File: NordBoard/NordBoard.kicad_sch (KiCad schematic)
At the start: 3 parts

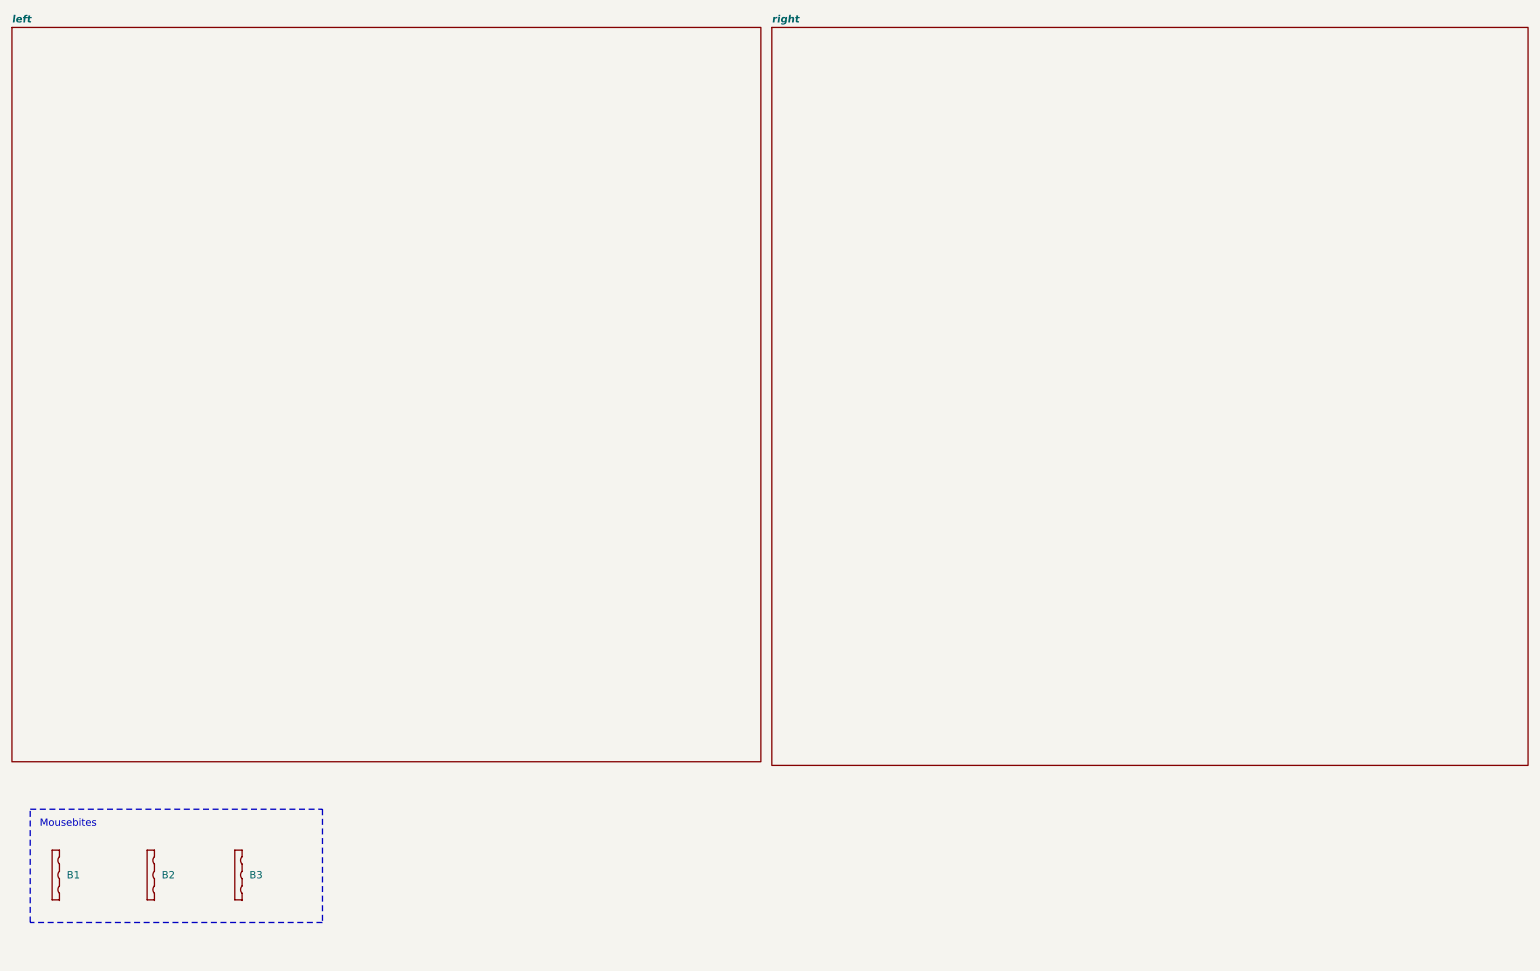
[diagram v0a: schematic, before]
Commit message: feat: implement mousebites
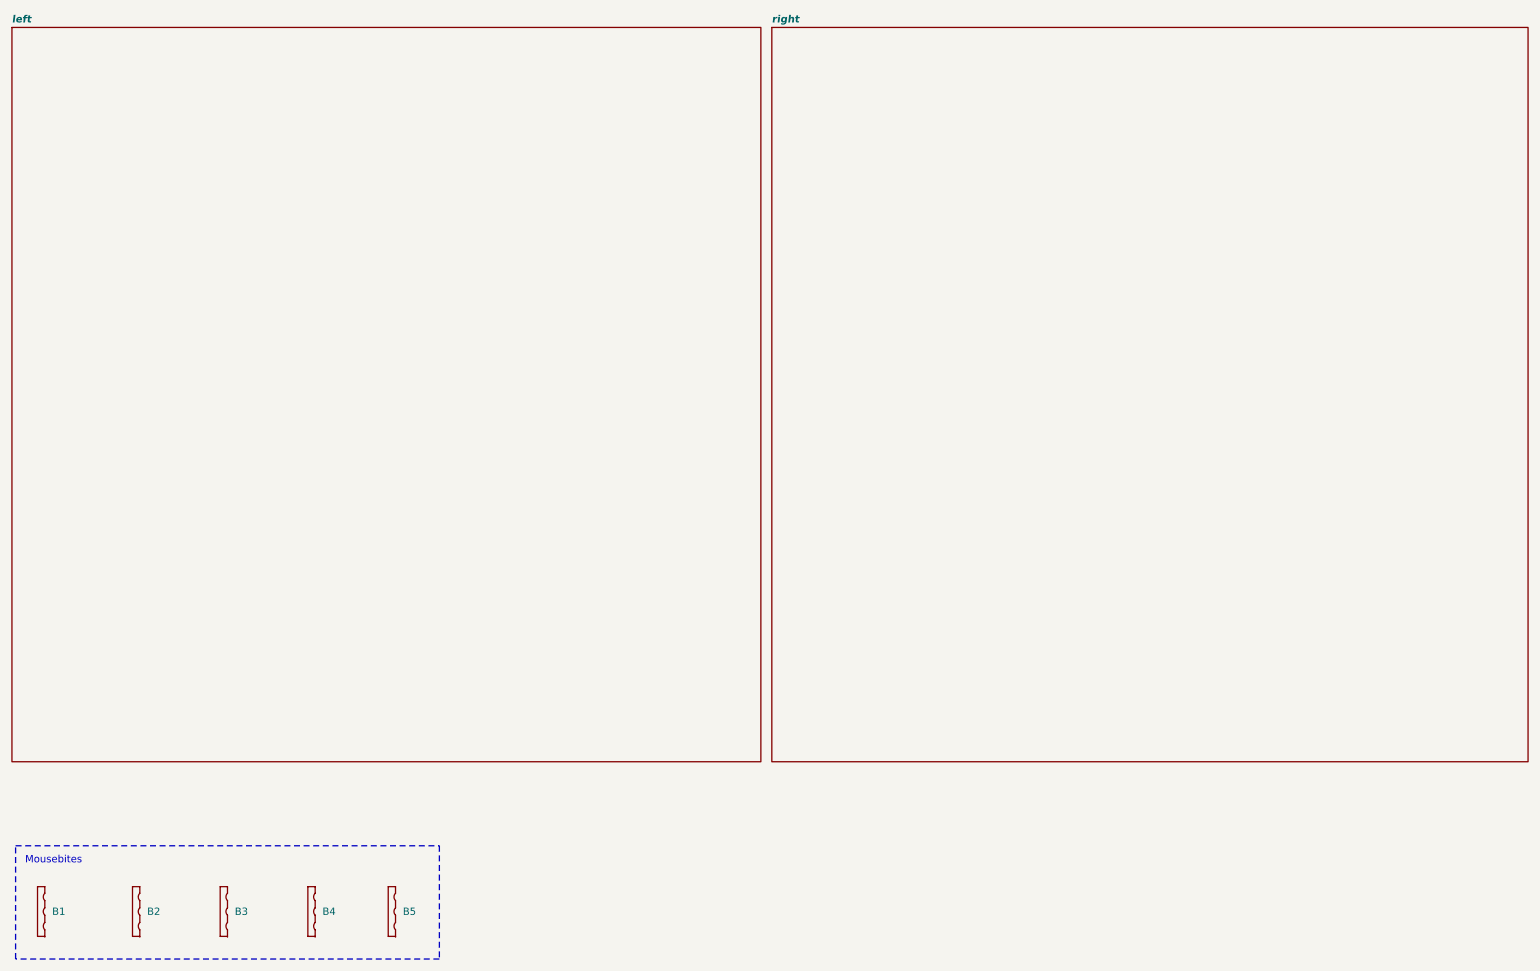
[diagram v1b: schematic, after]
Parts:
- added B4, B5: MouseBite, PCM_marbastlib-various:mousebites_2mm, symbol Mechanical:MouseBite
- B1, B2, B3: footprint Panelization:mouse-bite-5mm-slot -> PCM_marbastlib-various:mousebites_2mm
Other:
- moved on the sheet: B1, B2, B3
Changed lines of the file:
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@@
 	(paper "A4")
 	(rectangle
-		(start 19.05 165.1)
-		(end 69.85 184.785)
+		(start 16.51 171.45)
+		(end 90.17 191.135)
 		(stroke
 			(width 0)
@@
 	(text "Mousebites"
 		(exclude_from_sim no)
-		(at 25.654 167.64 0)
+		(at 23.114 173.99 0)
 		(effects
 			(font
@@
 	(symbol
 		(lib_id "Mechanical:MouseBite")
-		(at 54.61 176.53 0)
+		(at 52.07 182.88 0)
 		(unit 1)
 		(exclude_from_sim yes)
@@
 		(dnp no)
 		(property "Reference" "B3"
-			(at 57.15 176.53 0)
+			(at 54.61 182.88 0)
 			(effects
 				(font
@@
 		)
 		(property "Value" "MouseBite"
-			(at 57.15 177.8624 0)
-			(effects
-				(font
-					(size 1.27 1.27)
-				)
-				(justify left)
-				(hide yes)
-			)
-		)
-		(property "Footprint" "Panelization:mouse-bite-5mm-slot"
-			(at 54.61 176.53 0)
+			(at 54.61 184.2124 0)
+			(effects
+				(font
+					(size 1.27 1.27)
+				)
+				(justify left)
+				(hide yes)
+			)
+		)
+		(property "Footprint" "PCM_marbastlib-various:mousebites_2mm"
+			(at 52.07 182.88 0)
 			(effects
 				(font
@@
 		)
 		(property "Datasheet" "~"
-			(at 54.61 176.53 0)
+			(at 52.07 182.88 0)
 			(effects
 				(font
@@
 		)
 		(property "Description" "Mouse bites, break lines"
-			(at 54.61 176.53 0)
+			(at 52.07 182.88 0)
 			(effects
 				(font
@@
 	(symbol
 		(lib_id "Mechanical:MouseBite")
-		(at 39.37 176.53 0)
+		(at 36.83 182.88 0)
 		(unit 1)
 		(exclude_from_sim yes)
@@
 		(dnp no)
 		(property "Reference" "B2"
-			(at 41.91 176.53 0)
+			(at 39.37 182.88 0)
 			(effects
 				(font
@@
 		)
 		(property "Value" "MouseBite"
-			(at 41.91 177.8624 0)
-			(effects
-				(font
-					(size 1.27 1.27)
-				)
-				(justify left)
-				(hide yes)
-			)
-		)
-		(property "Footprint" "Panelization:mouse-bite-5mm-slot"
-			(at 39.37 176.53 0)
+			(at 39.37 184.2124 0)
+			(effects
+				(font
+					(size 1.27 1.27)
+				)
+				(justify left)
+				(hide yes)
+			)
+		)
+		(property "Footprint" "PCM_marbastlib-various:mousebites_2mm"
+			(at 36.83 182.88 0)
 			(effects
 				(font
@@
 		)
 		(property "Datasheet" "~"
-			(at 39.37 176.53 0)
+			(at 36.83 182.88 0)
 			(effects
 				(font
@@
 		)
 		(property "Description" "Mouse bites, break lines"
-			(at 39.37 176.53 0)
+			(at 36.83 182.88 0)
 			(effects
 				(font
@@
 	(symbol
 		(lib_id "Mechanical:MouseBite")
-		(at 22.86 176.53 0)
+		(at 20.32 182.88 0)
 		(unit 1)
 		(exclude_from_sim yes)
@@
 		(dnp no)
 		(property "Reference" "B1"
-			(at 25.4 176.53 0)
+			(at 22.86 182.88 0)
 			(effects
 				(font
@@
 		)
 		(property "Value" "MouseBite"
-			(at 25.4 177.8624 0)
-			(effects
-				(font
-					(size 1.27 1.27)
-				)
-				(justify left)
-				(hide yes)
-			)
-		)
-		(property "Footprint" "Panelization:mouse-bite-5mm-slot"
-			(at 22.86 176.53 0)
+			(at 22.86 184.2124 0)
+			(effects
+				(font
+					(size 1.27 1.27)
+				)
+				(justify left)
+				(hide yes)
+			)
+		)
+		(property "Footprint" "PCM_marbastlib-various:mousebites_2mm"
+			(at 20.32 182.88 0)
 			(effects
 				(font
@@
 		)
 		(property "Datasheet" "~"
-			(at 22.86 176.53 0)
+			(at 20.32 182.88 0)
 			(effects
 				(font
@@
 		)
 		(property "Description" "Mouse bites, break lines"
-			(at 22.86 176.53 0)
+			(at 20.32 182.88 0)
 			(effects
 				(font
@@
 				(path "/7cf7f72d-7ab1-4807-b592-339093d5ca44"
 					(reference "B1")
+					(unit 1)
+				)
+			)
+		)
+	)
+	(symbol
+		(lib_id "Mechanical:MouseBite")
+		(at 81.28 182.88 0)
+		(unit 1)
+		(exclude_from_sim yes)
+		(in_bom no)
+		(on_board yes)
+		(dnp no)
+		(property "Reference" "B5"
+			(at 83.82 182.88 0)
+			(effects
+				(font
+					(size 1.27 1.27)
+				)
+				(justify left)
+			)
+		)
+		(property "Value" "MouseBite"
+			(at 83.82 184.2124 0)
+			(effects
+				(font
+					(size 1.27 1.27)
+				)
+				(justify left)
+				(hide yes)
+			)
+		)
+		(property "Footprint" "PCM_marbastlib-various:mousebites_2mm"
+			(at 81.28 182.88 0)
+			(effects
+				(font
+					(size 1.27 1.27)
+				)
+				(hide yes)
+			)
+		)
+		(property "Datasheet" "~"
+			(at 81.28 182.88 0)
+			(effects
+				(font
+					(size 1.27 1.27)
+				)
+				(hide yes)
+			)
+		)
+		(property "Description" "Mouse bites, break lines"
+			(at 81.28 182.88 0)
+			(effects
+				(font
+					(size 1.27 1.27)
+				)
+				(hide yes)
+			)
+		)
+		(instances
+			(project "NordBoard"
+				(path "/7cf7f72d-7ab1-4807-b592-339093d5ca44"
+					(reference "B5")
+					(unit 1)
+				)
+			)
+		)
+	)
+	(symbol
+		(lib_id "Mechanical:MouseBite")
+		(at 67.31 182.88 0)
+		(unit 1)
+		(exclude_from_sim yes)
+		(in_bom no)
+		(on_board yes)
+		(dnp no)
+		(property "Reference" "B4"
+			(at 69.85 182.88 0)
+			(effects
+				(font
+					(size 1.27 1.27)
+				)
+				(justify left)
+			)
+		)
+		(property "Value" "MouseBite"
+			(at 69.85 184.2124 0)
+			(effects
+				(font
+					(size 1.27 1.27)
+				)
+				(justify left)
+				(hide yes)
+			)
+		)
+		(property "Footprint" "PCM_marbastlib-various:mousebites_2mm"
+			(at 67.31 182.88 0)
+			(effects
+				(font
+					(size 1.27 1.27)
+				)
+				(hide yes)
+			)
+		)
+		(property "Datasheet" "~"
+			(at 67.31 182.88 0)
+			(effects
+				(font
+					(size 1.27 1.27)
+				)
+				(hide yes)
+			)
+		)
+		(property "Description" "Mouse bites, break lines"
+			(at 67.31 182.88 0)
+			(effects
+				(font
+					(size 1.27 1.27)
+				)
+				(hide yes)
+			)
+		)
+		(instances
+			(project "NordBoard"
+				(path "/7cf7f72d-7ab1-4807-b592-339093d5ca44"
+					(reference "B4")
 					(unit 1)
 				)
@@
 	(sheet
 		(at 147.955 29.21)
-		(size 131.445 128.27)
+		(size 131.445 127.635)
 		(exclude_from_sim no)
 		(in_bom yes)
@@
 		)
 		(property "Sheetfile" "side.kicad_sch"
-			(at 147.955 158.0646 0)
-			(effects
-				(font
+			(at 147.955 157.4296 0)
+			(effects
+				(font

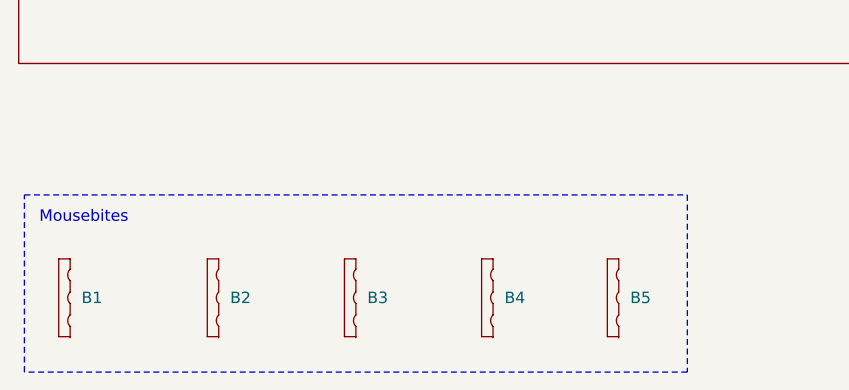
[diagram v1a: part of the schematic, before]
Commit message: feat: finish PCB awaiting peer review + silkscreen
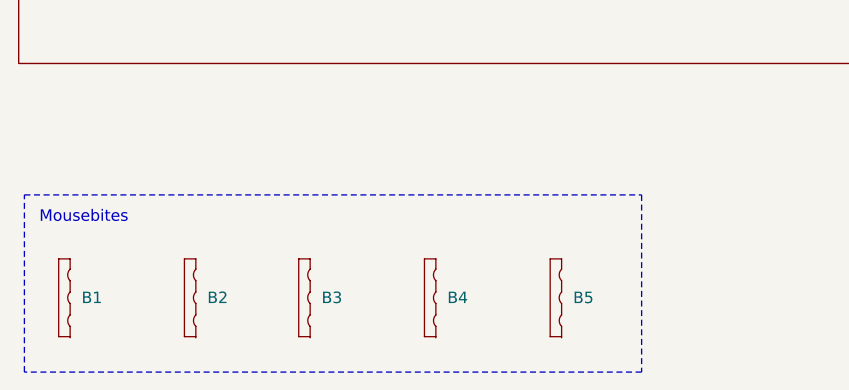
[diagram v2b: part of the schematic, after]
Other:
- moved on the sheet: B2, B3, B4, B5
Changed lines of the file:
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@@
 	(rectangle
 		(start 16.51 171.45)
-		(end 90.17 191.135)
+		(end 85.09 191.135)
 		(stroke
 			(width 0)
@@
 	(symbol
 		(lib_id "Mechanical:MouseBite")
-		(at 52.07 182.88 0)
+		(at 46.99 182.88 0)
 		(unit 1)
 		(exclude_from_sim yes)
@@
 		(dnp no)
 		(property "Reference" "B3"
-			(at 54.61 182.88 0)
-			(effects
-				(font
-					(size 1.27 1.27)
-				)
-				(justify left)
-			)
-		)
-		(property "Value" "MouseBite"
-			(at 54.61 184.2124 0)
-			(effects
-				(font
-					(size 1.27 1.27)
-				)
-				(justify left)
-				(hide yes)
-			)
-		)
-		(property "Footprint" "PCM_marbastlib-various:mousebites_2mm"
-			(at 52.07 182.88 0)
-			(effects
-				(font
-					(size 1.27 1.27)
-				)
-				(hide yes)
-			)
-		)
-		(property "Datasheet" "~"
-			(at 52.07 182.88 0)
-			(effects
-				(font
-					(size 1.27 1.27)
-				)
-				(hide yes)
-			)
-		)
-		(property "Description" "Mouse bites, break lines"
-			(at 52.07 182.88 0)
+			(at 49.53 182.88 0)
+			(effects
+				(font
+					(size 1.27 1.27)
+				)
+				(justify left)
+			)
+		)
+		(property "Value" "MouseBite"
+			(at 49.53 184.2124 0)
+			(effects
+				(font
+					(size 1.27 1.27)
+				)
+				(justify left)
+				(hide yes)
+			)
+		)
+		(property "Footprint" "PCM_marbastlib-various:mousebites_2mm"
+			(at 46.99 182.88 0)
+			(effects
+				(font
+					(size 1.27 1.27)
+				)
+				(hide yes)
+			)
+		)
+		(property "Datasheet" "~"
+			(at 46.99 182.88 0)
+			(effects
+				(font
+					(size 1.27 1.27)
+				)
+				(hide yes)
+			)
+		)
+		(property "Description" "Mouse bites, break lines"
+			(at 46.99 182.88 0)
 			(effects
 				(font
@@
 	(symbol
 		(lib_id "Mechanical:MouseBite")
-		(at 36.83 182.88 0)
+		(at 34.29 182.88 0)
 		(unit 1)
 		(exclude_from_sim yes)
@@
 		(dnp no)
 		(property "Reference" "B2"
-			(at 39.37 182.88 0)
-			(effects
-				(font
-					(size 1.27 1.27)
-				)
-				(justify left)
-			)
-		)
-		(property "Value" "MouseBite"
-			(at 39.37 184.2124 0)
-			(effects
-				(font
-					(size 1.27 1.27)
-				)
-				(justify left)
-				(hide yes)
-			)
-		)
-		(property "Footprint" "PCM_marbastlib-various:mousebites_2mm"
 			(at 36.83 182.88 0)
 			(effects
@@
 					(size 1.27 1.27)
 				)
-				(hide yes)
-			)
-		)
-		(property "Datasheet" "~"
-			(at 36.83 182.88 0)
-			(effects
-				(font
-					(size 1.27 1.27)
-				)
-				(hide yes)
-			)
-		)
-		(property "Description" "Mouse bites, break lines"
-			(at 36.83 182.88 0)
+				(justify left)
+			)
+		)
+		(property "Value" "MouseBite"
+			(at 36.83 184.2124 0)
+			(effects
+				(font
+					(size 1.27 1.27)
+				)
+				(justify left)
+				(hide yes)
+			)
+		)
+		(property "Footprint" "PCM_marbastlib-various:mousebites_2mm"
+			(at 34.29 182.88 0)
+			(effects
+				(font
+					(size 1.27 1.27)
+				)
+				(hide yes)
+			)
+		)
+		(property "Datasheet" "~"
+			(at 34.29 182.88 0)
+			(effects
+				(font
+					(size 1.27 1.27)
+				)
+				(hide yes)
+			)
+		)
+		(property "Description" "Mouse bites, break lines"
+			(at 34.29 182.88 0)
 			(effects
 				(font
@@
 	(symbol
 		(lib_id "Mechanical:MouseBite")
-		(at 81.28 182.88 0)
+		(at 74.93 182.88 0)
 		(unit 1)
 		(exclude_from_sim yes)
@@
 		(dnp no)
 		(property "Reference" "B5"
-			(at 83.82 182.88 0)
-			(effects
-				(font
-					(size 1.27 1.27)
-				)
-				(justify left)
-			)
-		)
-		(property "Value" "MouseBite"
-			(at 83.82 184.2124 0)
-			(effects
-				(font
-					(size 1.27 1.27)
-				)
-				(justify left)
-				(hide yes)
-			)
-		)
-		(property "Footprint" "PCM_marbastlib-various:mousebites_2mm"
-			(at 81.28 182.88 0)
-			(effects
-				(font
-					(size 1.27 1.27)
-				)
-				(hide yes)
-			)
-		)
-		(property "Datasheet" "~"
-			(at 81.28 182.88 0)
-			(effects
-				(font
-					(size 1.27 1.27)
-				)
-				(hide yes)
-			)
-		)
-		(property "Description" "Mouse bites, break lines"
-			(at 81.28 182.88 0)
+			(at 77.47 182.88 0)
+			(effects
+				(font
+					(size 1.27 1.27)
+				)
+				(justify left)
+			)
+		)
+		(property "Value" "MouseBite"
+			(at 77.47 184.2124 0)
+			(effects
+				(font
+					(size 1.27 1.27)
+				)
+				(justify left)
+				(hide yes)
+			)
+		)
+		(property "Footprint" "PCM_marbastlib-various:mousebites_2mm"
+			(at 74.93 182.88 0)
+			(effects
+				(font
+					(size 1.27 1.27)
+				)
+				(hide yes)
+			)
+		)
+		(property "Datasheet" "~"
+			(at 74.93 182.88 0)
+			(effects
+				(font
+					(size 1.27 1.27)
+				)
+				(hide yes)
+			)
+		)
+		(property "Description" "Mouse bites, break lines"
+			(at 74.93 182.88 0)
 			(effects
 				(font
@@
 	(symbol
 		(lib_id "Mechanical:MouseBite")
-		(at 67.31 182.88 0)
+		(at 60.96 182.88 0)
 		(unit 1)
 		(exclude_from_sim yes)
@@
 		(dnp no)
 		(property "Reference" "B4"
-			(at 69.85 182.88 0)
-			(effects
-				(font
-					(size 1.27 1.27)
-				)
-				(justify left)
-			)
-		)
-		(property "Value" "MouseBite"
-			(at 69.85 184.2124 0)
-			(effects
-				(font
-					(size 1.27 1.27)
-				)
-				(justify left)
-				(hide yes)
-			)
-		)
-		(property "Footprint" "PCM_marbastlib-various:mousebites_2mm"
-			(at 67.31 182.88 0)
-			(effects
-				(font
-					(size 1.27 1.27)
-				)
-				(hide yes)
-			)
-		)
-		(property "Datasheet" "~"
-			(at 67.31 182.88 0)
-			(effects
-				(font
-					(size 1.27 1.27)
-				)
-				(hide yes)
-			)
-		)
-		(property "Description" "Mouse bites, break lines"
-			(at 67.31 182.88 0)
-			(effects
-				(font
+			(at 63.5 182.88 0)
+			(effects
+				(font
+					(size 1.27 1.27)
+				)
+				(justify left)
+			)
+		)
+		(property "Value" "MouseBite"
+			(at 63.5 184.2124 0)
+			(effects
+				(font
+					(size 1.27 1.27)
+				)
+				(justify left)
+				(hide yes)
+			)
+		)
+		(property "Footprint" "PCM_marbastlib-various:mousebites_2mm"
+			(at 60.96 182.88 0)
+			(effects
+				(font
+					(size 1.27 1.27)
+				)
+				(hide yes)
+			)
+		)
+		(property "Datasheet" "~"
+			(at 60.96 182.88 0)
+			(effects
+				(font
+					(size 1.27 1.27)
+				)
+				(hide yes)
+			)
+		)
+		(property "Description" "Mouse bites, break lines"
+			(at 60.96 182.88 0)
+			(effects
+				(font
